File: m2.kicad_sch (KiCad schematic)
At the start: 22 parts, among them J5 Bus_M.2_1-2199230-6, U10 AP22615AWU-7, Y1 Oscillator_32.768kHz_OK2EL89C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

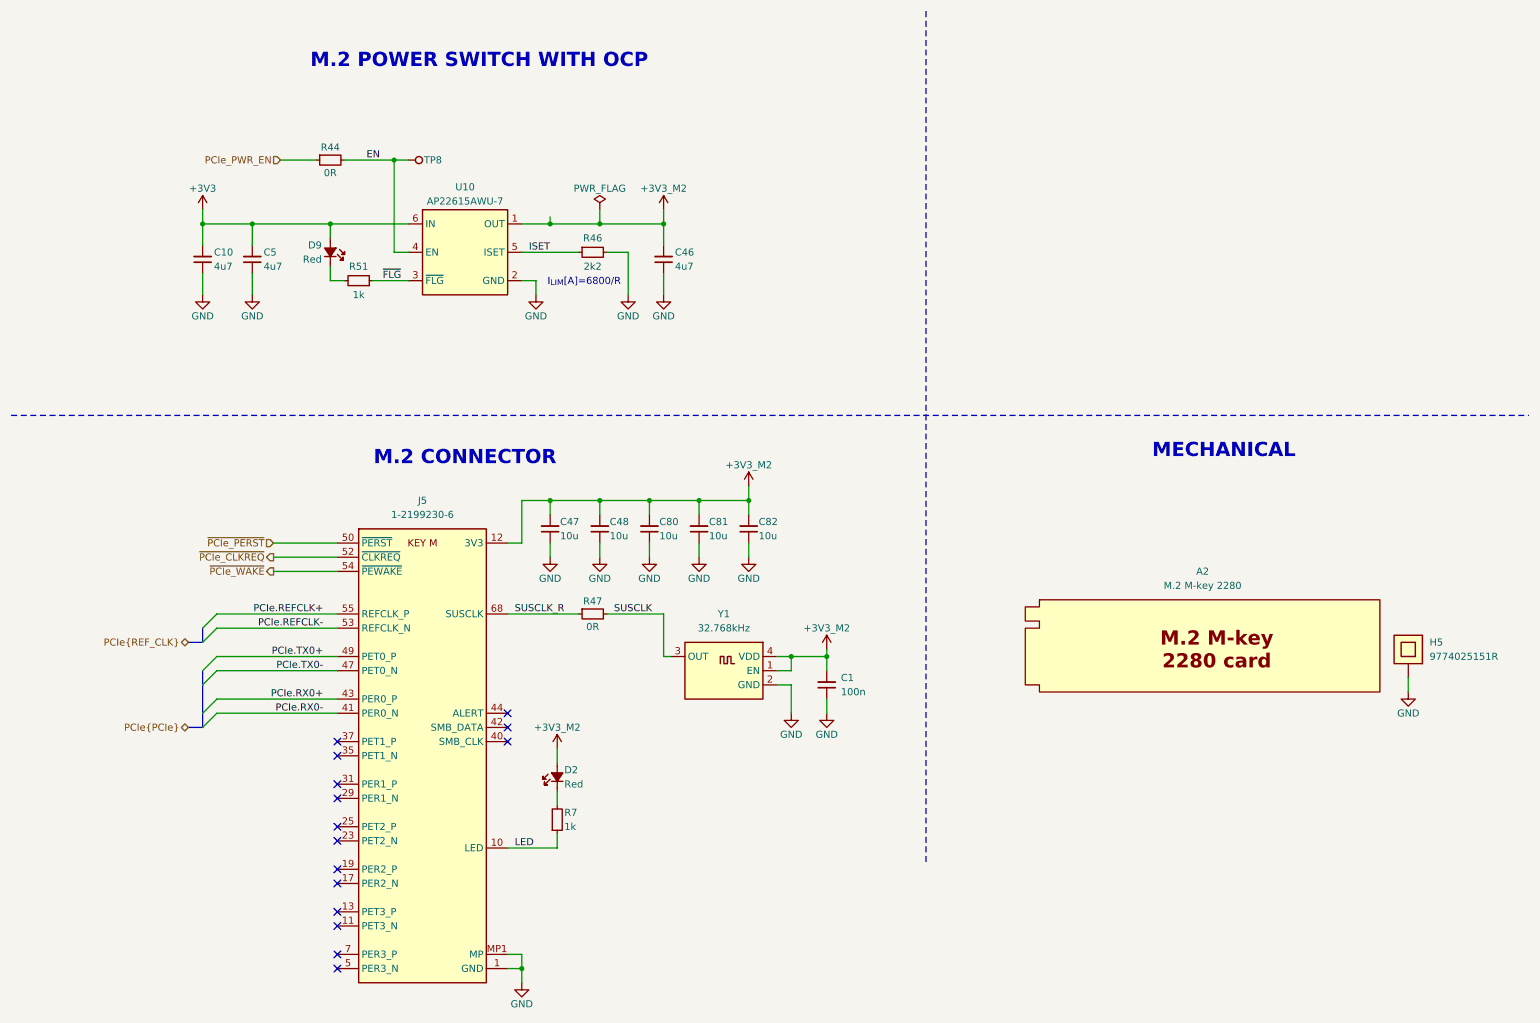
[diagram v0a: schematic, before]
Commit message: [#3] WIP: Clear ERC, re-annotate schematic
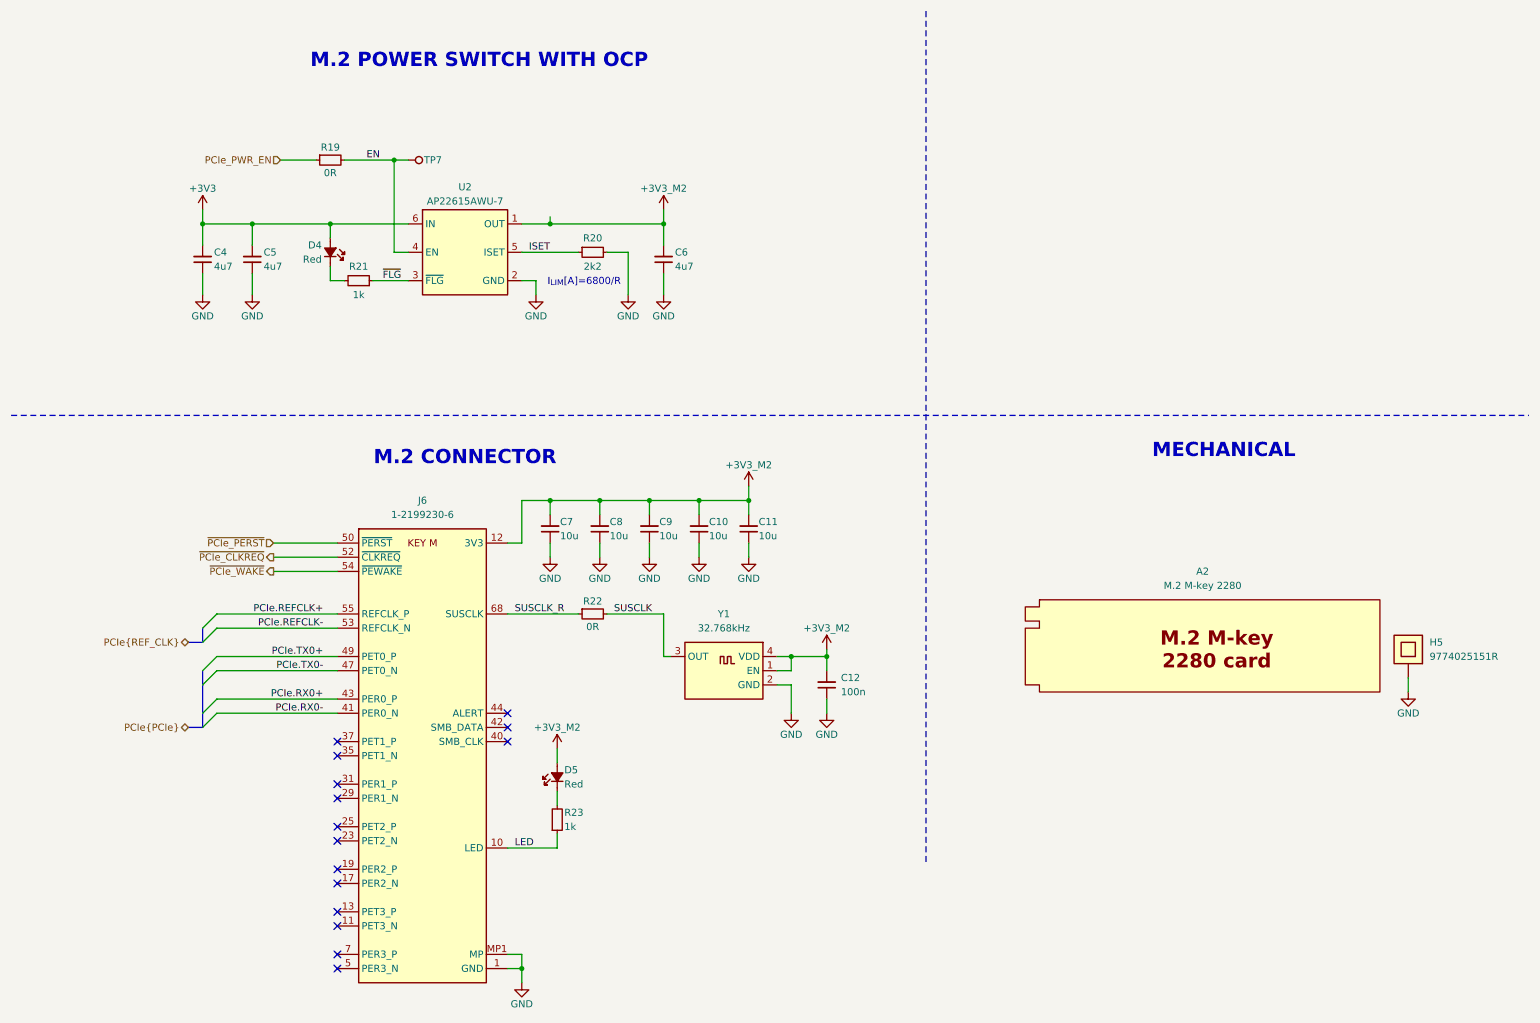
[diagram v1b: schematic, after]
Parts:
- renumbered C81 to C10, C82 to C11, C1 to C12, C10 to C4, C46 to C6, C47 to C7, C48 to C8, C80 to C9, D9 to D4, D2 to D5, J5 to J6, R44 to R19, R46 to R20, R51 to R21, R47 to R22, R7 to R23, TP8 to TP7, U10 to U2

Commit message: [#3] Re-annotate schematic
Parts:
- renumbered C4 to C30, C5 to C31, C6 to C32, C7 to C33, C8 to C34, C9 to C35, C10 to C36, C11 to C37, C12 to C38, R19 to R31, R20 to R32, R21 to R33, R22 to R34, R23 to R35, U2 to U6
